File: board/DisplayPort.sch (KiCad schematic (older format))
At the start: 13 parts, among them J8 DISPLAY_PORT, J9 DISPLAY_PORT

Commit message: Issue #1767 - Feedback changes
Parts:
- added C47, C49: 0.01uF, ~, symbol C
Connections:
- net GND: now also C47.2, C49.2
- net at D3.2 (K), J8.20 (DP_PWR): now also C47.1
- net at D11.2 (K), J9.20 (DP_PWR), R25.1: now also C49.1
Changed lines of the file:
@@
 Sheet 6 12
 Title "HDMI2USB"
-Date "10 apr 2015"
+Date "20 apr 2015"
 Rev "Rev2"
 Comp ""
@@
 	2900 3750 3350 3750
 Wire Wire Line
-	3300 3950 3300 4450
+	3300 3950 3300 4500
 Wire Wire Line
 	3300 4450 3650 4450
@@
 Text Notes 4150 4350 0    60   ~ 0
 500mA
+$Comp
+L C C47
+U 1 1 55352168
+P 3300 4700
+F 0 "C47" H 3300 4800 40  0000 L CNN
+F 1 "0.01uF" H 3306 4615 40  0000 L CNN
+F 2 "~" H 3338 4550 30  0000 C CNN
+F 3 "~" H 3300 4700 60  0000 C CNN
+	1    3300 4700
+	1    0    0    -1
+$EndComp
+Connection ~ 3300 4450
+Text Label 3150 4950 0    39   ~ 0
+GND
+Wire Wire Line
+	3150 4950 3300 4950
+Wire Wire Line
+	3300 4950 3300 4900
+$Comp
+L C C49
+U 1 1 55352215
+P 7650 4700
+F 0 "C49" H 7650 4800 40  0000 L CNN
+F 1 "0.01uF" H 7656 4615 40  0000 L CNN
+F 2 "~" H 7688 4550 30  0000 C CNN
+F 3 "~" H 7650 4700 60  0000 C CNN
+	1    7650 4700
+	1    0    0    -1
+$EndComp
+Text Label 7500 4950 0    39   ~ 0
+GND
+Wire Wire Line
+	7500 4950 7650 4950
+Wire Wire Line
+	7650 4950 7650 4900
+Wire Wire Line
+	7650 4450 7650 4500
 $EndSCHEMATC

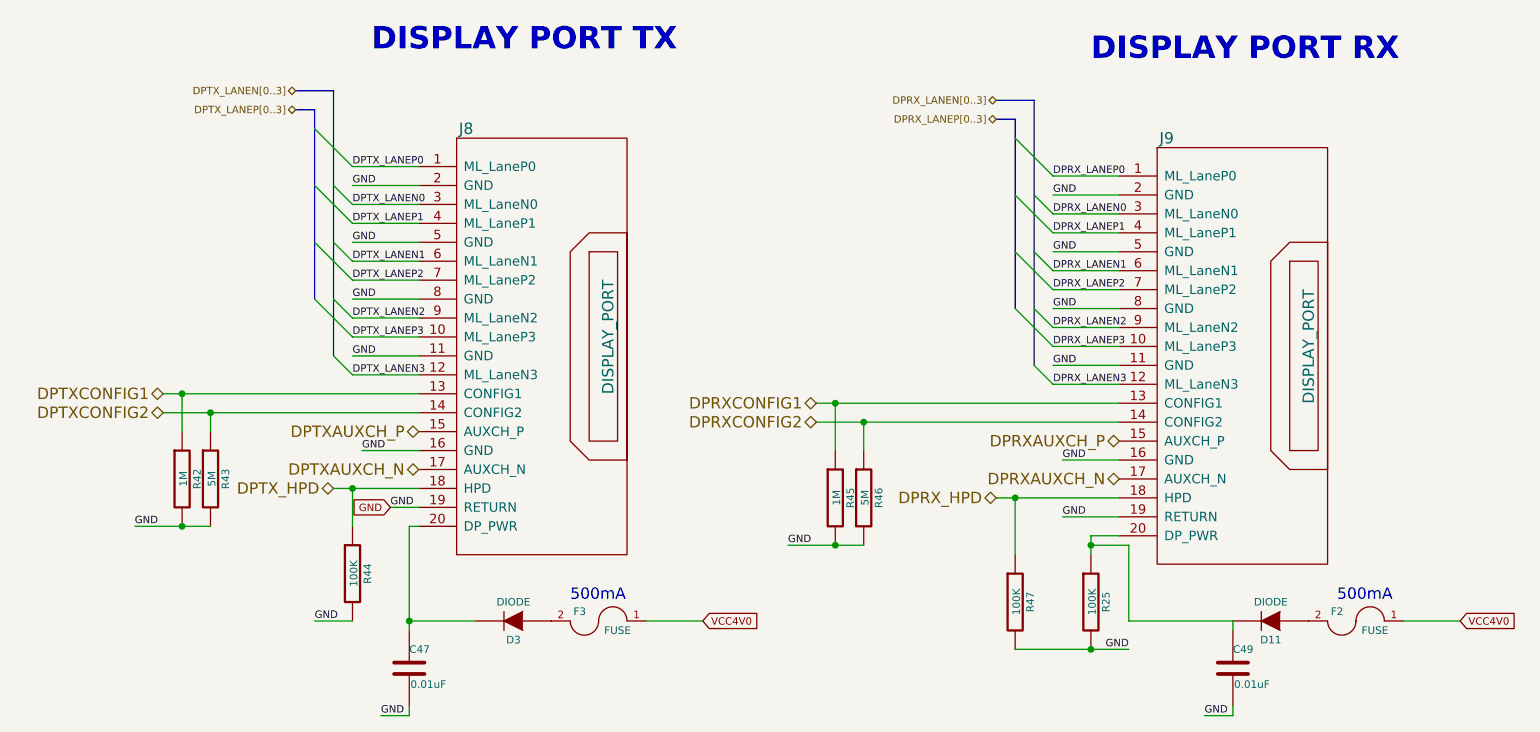
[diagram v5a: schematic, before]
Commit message: Issue #1961 - Adding initial "populate" field to all components.
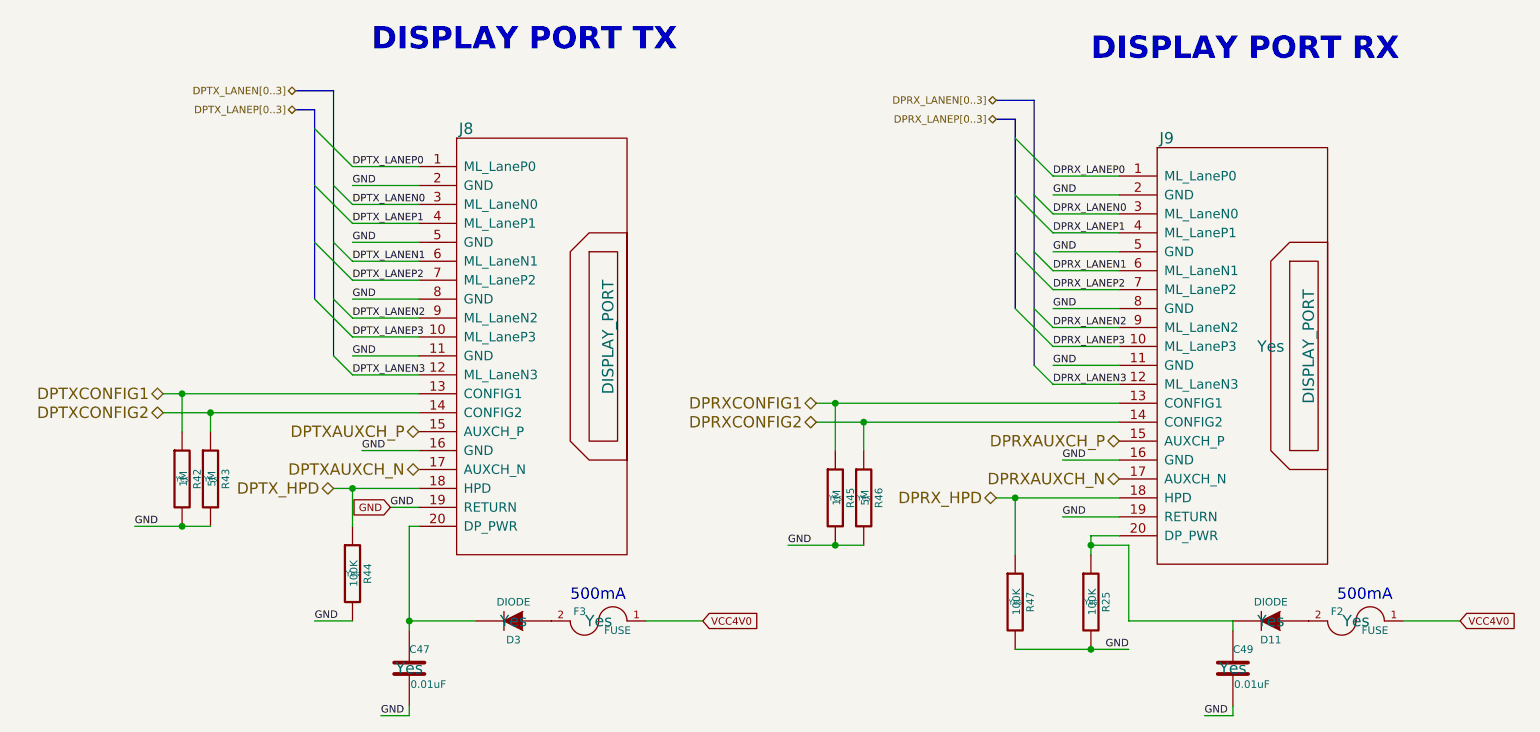
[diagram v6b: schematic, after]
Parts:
- C47, C49, D11, D3, F2, F3, J8, J9, R25, R42, R43, R44, R45, R46, R47: Populate (none) -> Yes
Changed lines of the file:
@@
 Sheet 6 12
 Title "HDMI2USB"
-Date "5 may 2015"
+Date "5 jul 2015"
 Rev "Rev2"
 Comp ""
@@
 F 2 "~" H 4150 2950 60  0000 C CNN
 F 3 "~" H 4150 2950 60  0000 C CNN
+F 4 "Yes" H 4200 2950 60  0001 C CNN "Populate"
 	1    4200 2950
 	1    0    0    -1
@@
 F 2 "~" H 7850 3000 60  0000 C CNN
 F 3 "~" H 7850 3000 60  0000 C CNN
+F 4 "Yes" H 7850 3000 60  0000 C CNN "Populate"
 	1    7900 3000
 	1    0    0    -1
@@
 F 2 "~" V 6830 4350 30  0000 C CNN
 F 3 "~" H 6900 4350 30  0000 C CNN
+F 4 "Yes" H 6900 4350 30  0000 C CNN "Populate"
 	1    6900 4350
 	1    0    0    -1
@@
 F 2 "~" H 4300 4450 60  0000 C CNN
 F 3 "~" H 4300 4450 60  0000 C CNN
+F 4 "Yes" H 4300 4450 60  0000 C CNN "Populate"
 	1    4300 4450
 	-1   0    0    -1
@@
 F 2 "~" V 2030 3700 30  0000 C CNN
 F 3 "~" H 2100 3700 30  0000 C CNN
+F 4 "Yes" H 2100 3700 30  0000 C CNN "Populate"
 	1    2100 3700
 	1    0    0    -1
@@
 F 2 "~" V 2180 3700 30  0000 C CNN
 F 3 "~" H 2250 3700 30  0000 C CNN
+F 4 "Yes" H 2250 3700 30  0000 C CNN "Populate"
 	1    2250 3700
 	1    0    0    -1
@@
 F 2 "~" V 5480 3800 30  0000 C CNN
 F 3 "~" H 5550 3800 30  0000 C CNN
+F 4 "Yes" H 5550 3800 30  0000 C CNN "Populate"
 	1    5550 3800
 	1    0    0    -1
@@
 F 2 "~" V 5630 3800 30  0000 C CNN
 F 3 "~" H 5700 3800 30  0000 C CNN
+F 4 "Yes" H 5700 3800 30  0000 C CNN "Populate"
 	1    5700 3800
 	1    0    0    -1
@@
 F 2 "~" V 6430 4350 30  0000 C CNN
 F 3 "~" H 6500 4350 30  0000 C CNN
+F 4 "Yes" H 6500 4350 30  0000 C CNN "Populate"
 	1    6500 4350
 	1    0    0    -1
@@
 F 2 "~" V 2930 4200 30  0000 C CNN
 F 3 "~" H 3000 4200 30  0000 C CNN
+F 4 "Yes" H 3000 4200 30  0000 C CNN "Populate"
 	1    3000 4200
 	1    0    0    -1
@@
 F 2 "~" H 3850 4450 60  0000 C CNN
 F 3 "~" H 3850 4450 60  0000 C CNN
+F 4 "Yes" H 3850 4450 60  0000 C CNN "Populate"
 	1    3850 4450
 	-1   0    0    1
@@
 F 2 "~" H 8300 4450 60  0000 C CNN
 F 3 "~" H 8300 4450 60  0000 C CNN
+F 4 "Yes" H 8300 4450 60  0000 C CNN "Populate"
 	1    8300 4450
 	-1   0    0    -1
@@
 F 2 "~" H 7850 4450 60  0000 C CNN
 F 3 "~" H 7850 4450 60  0000 C CNN
+F 4 "Yes" H 7850 4450 60  0000 C CNN "Populate"
 	1    7850 4450
 	-1   0    0    1
@@
 F 2 "~" H 3338 4550 30  0000 C CNN
 F 3 "~" H 3300 4700 60  0000 C CNN
+F 4 "Yes" H 3300 4700 60  0000 C CNN "Populate"
 	1    3300 4700
 	1    0    0    -1
@@
 F 2 "~" H 7688 4550 30  0000 C CNN
 F 3 "~" H 7650 4700 60  0000 C CNN
+F 4 "Yes" H 7650 4700 60  0000 C CNN "Populate"
 	1    7650 4700
 	1    0    0    -1
